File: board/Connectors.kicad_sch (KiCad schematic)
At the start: 17 parts, among them J10 SLOT 4, J11 SLOT 1, J12 SLOT 5, J13 SLOT 2, J14 SPI Device 0, J15 SPI Device 4, J16 SPI Device 1, J17 SPI Device 5, J18 Audio Jack, J19 SPI Device 2, J20 SPI Device 6, J21 SPI Device 3, J22 SPI Device 7, J23 SLOT 3, J24 VIA Port A, J25 SP720APP, J9 SLOT 0

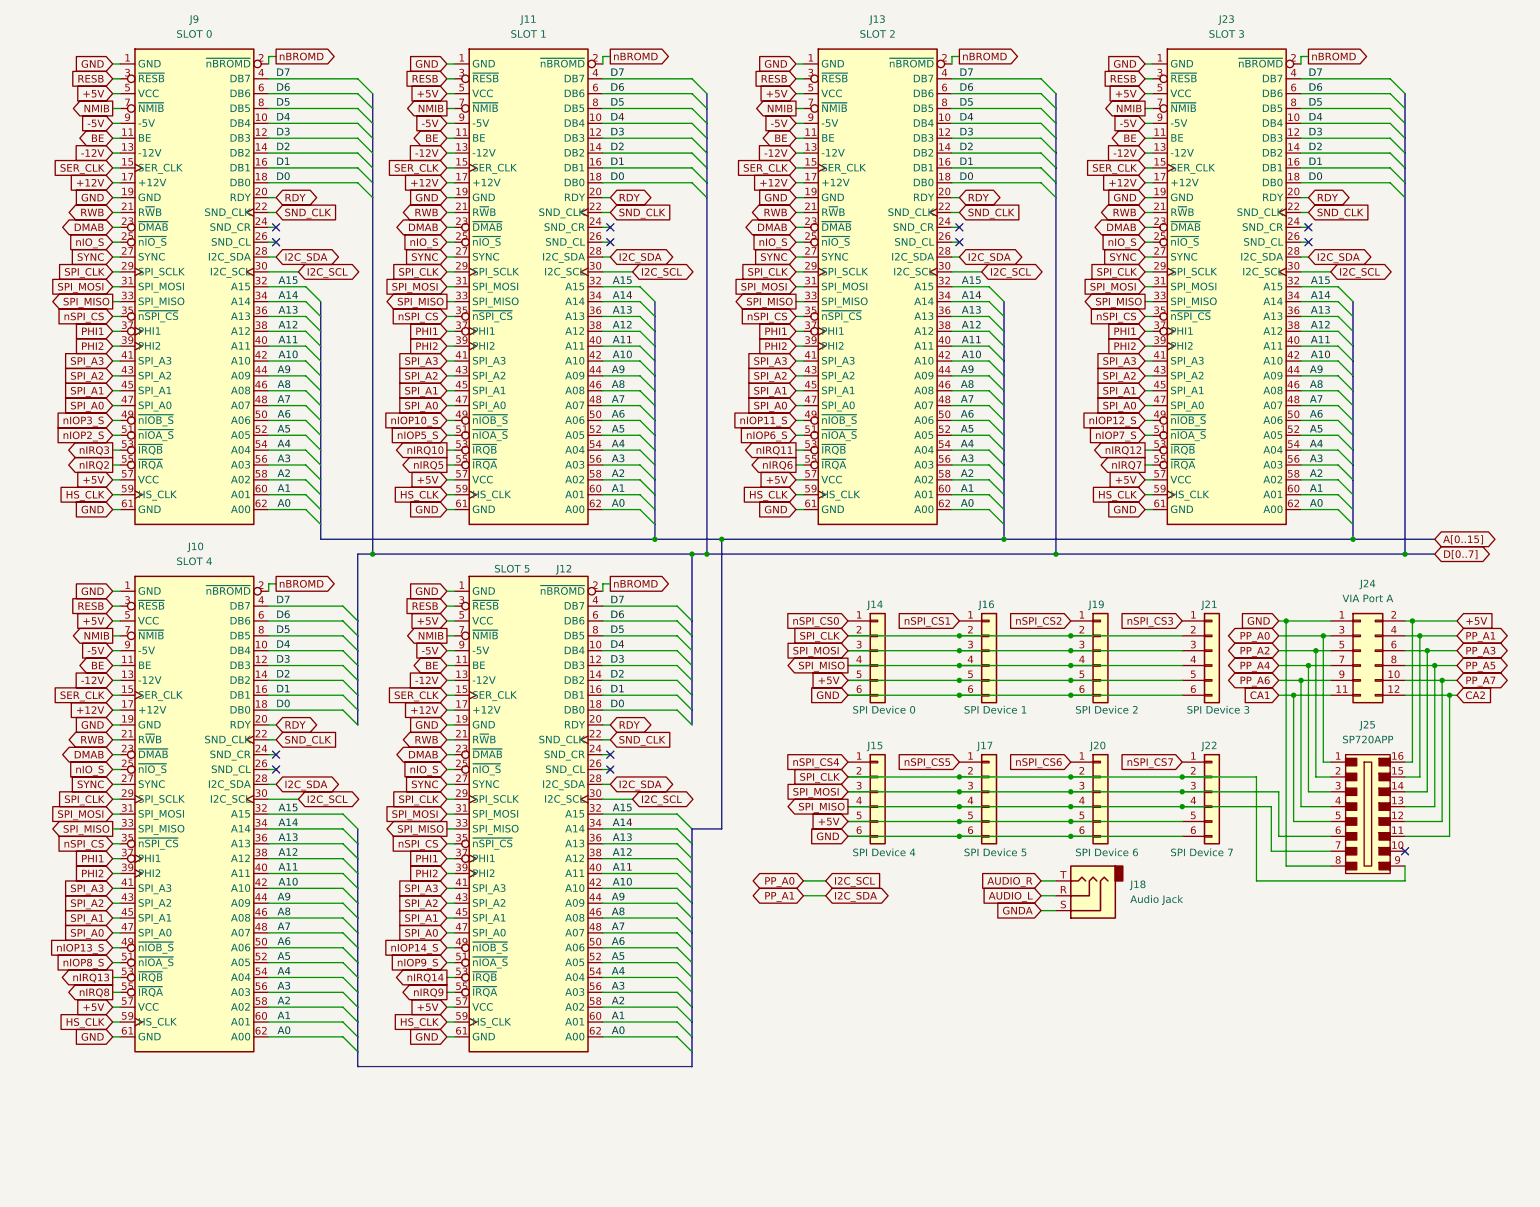
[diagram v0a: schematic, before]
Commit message: V2.0: wait states, GAL glue logic, serial clock and review fixes
Main board schematic:
- Replace the T4-T7 clock divider with RDY wait states. Fixed 7.16 MHz
  CPU clock; J36 selects 3.58 MHz for Rockwell parts. Waits are set per
  region through the write-only register at $FFF5 (reset = 3 waits).
- Move address decode, strobes, the wait-state generator, the IRQ
  encoder/latch/vector mux, ROM bank gating and DMA sync into seven GALs
  (U81-U86 ATF22V10C, U87 ATF16V8C), removing 29 ICs. CUPL sources,
  JEDECs and notes are in board/PLDs/V2.
- 1.8432 MHz serial clock, soft-power latch, -5V regulator, bulk caps,
  pull-ups, audio coupling/decoupling, GNDA tie, read-only Z register
  and other design-review fixes.
- New WaitStates and Support sheets; project symbol library
  hydra16.kicad_sym with sym-lib-table.

PCB updated from the schematic. Includes pending changes to the counter,
bus breakout and memory daughter card projects.

Firmware:
- Remove S_REGISTER; T/U/V/W now at $FFF0-$FFF3 to match the hardware.
- Add math.s and sound.s (included by os_main.s).
- Rebuild the 65C02 ROM image.

Co-Authored-By: Claude Opus 5.5 <noreply@anthropic.com>
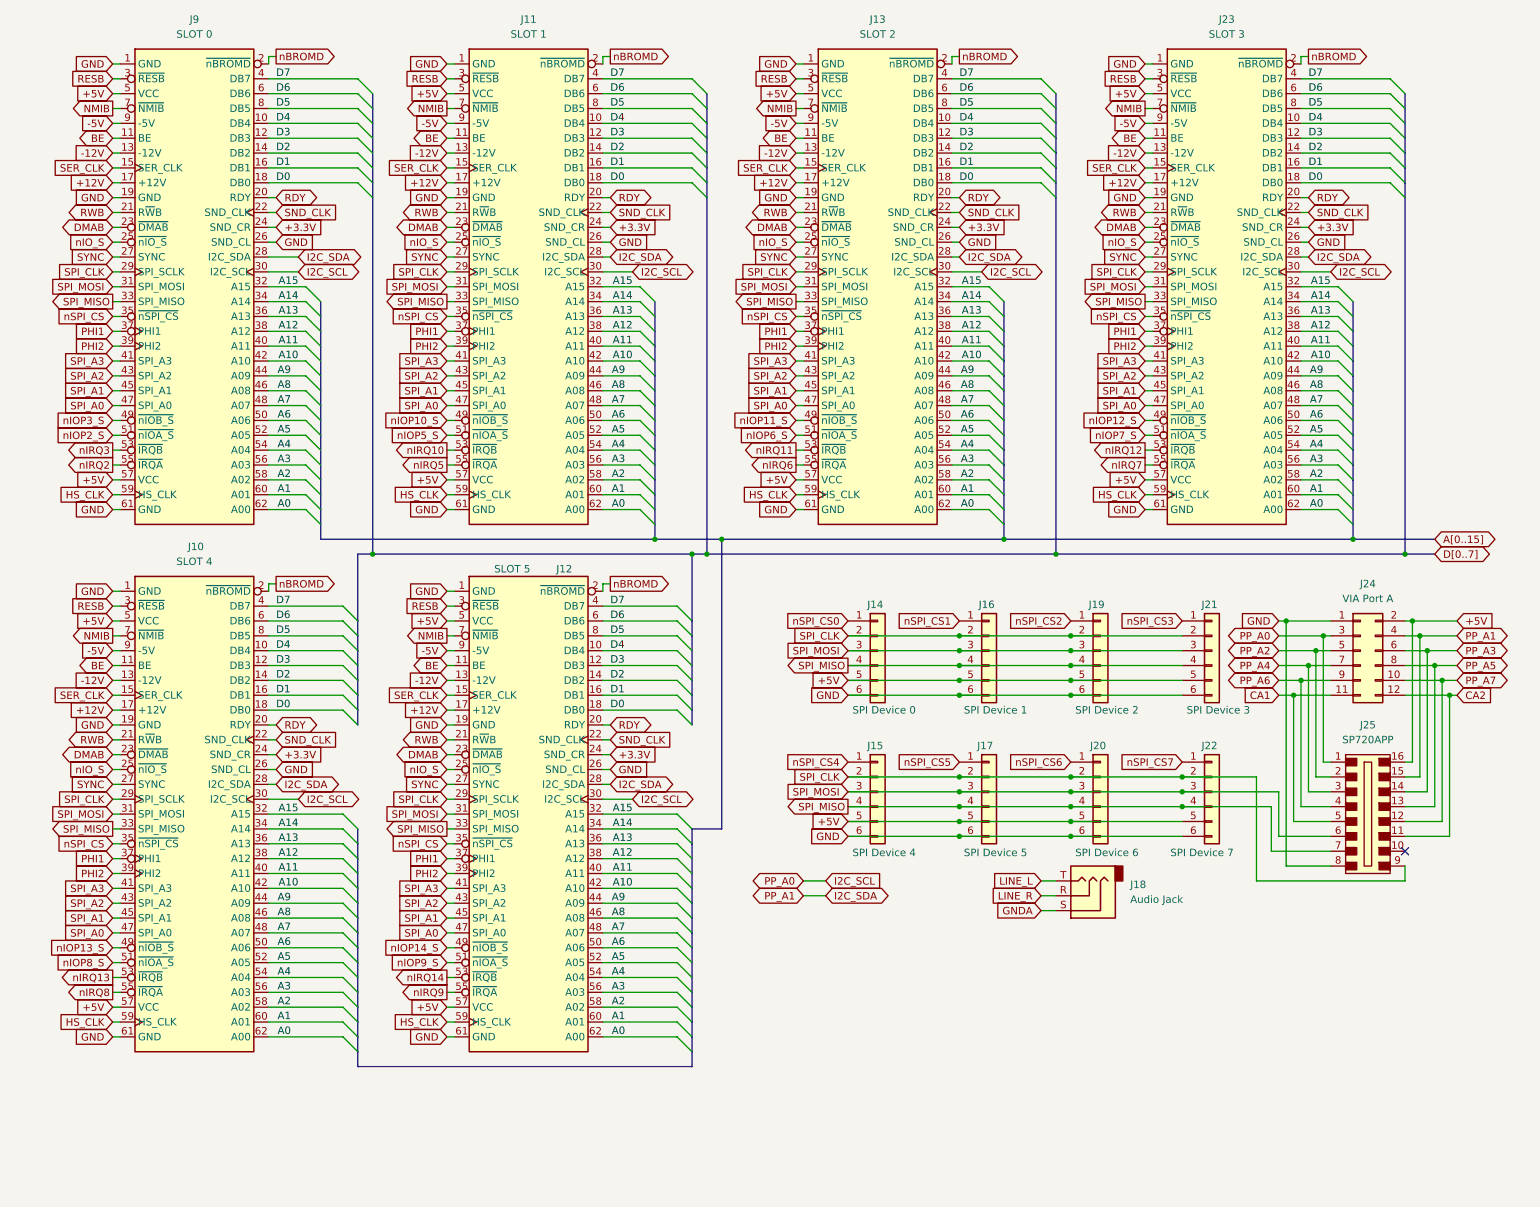
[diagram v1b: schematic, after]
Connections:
- net GND: now also J10.26 (SND_CL), J11.26 (SND_CL), J12.26 (SND_CL), J13.26 (SND_CL), J23.26 (SND_CL), J9.26 (SND_CL)
- net +3.3V: now reaches J11.24 (SND_CR)
- net +3.3V: now also J10.24 (SND_CR), J12.24 (SND_CR), J13.24 (SND_CR), J23.24 (SND_CR), J9.24 (SND_CR)
- net AUDIO_L renamed LINE_R
- net AUDIO_R renamed LINE_L
- no-connect marks 13 -> 1
